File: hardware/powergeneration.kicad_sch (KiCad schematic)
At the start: 36 parts, among them U11 TPS55340PWPR, U5 AOZ1284PI, U6 TL431BIDBZR

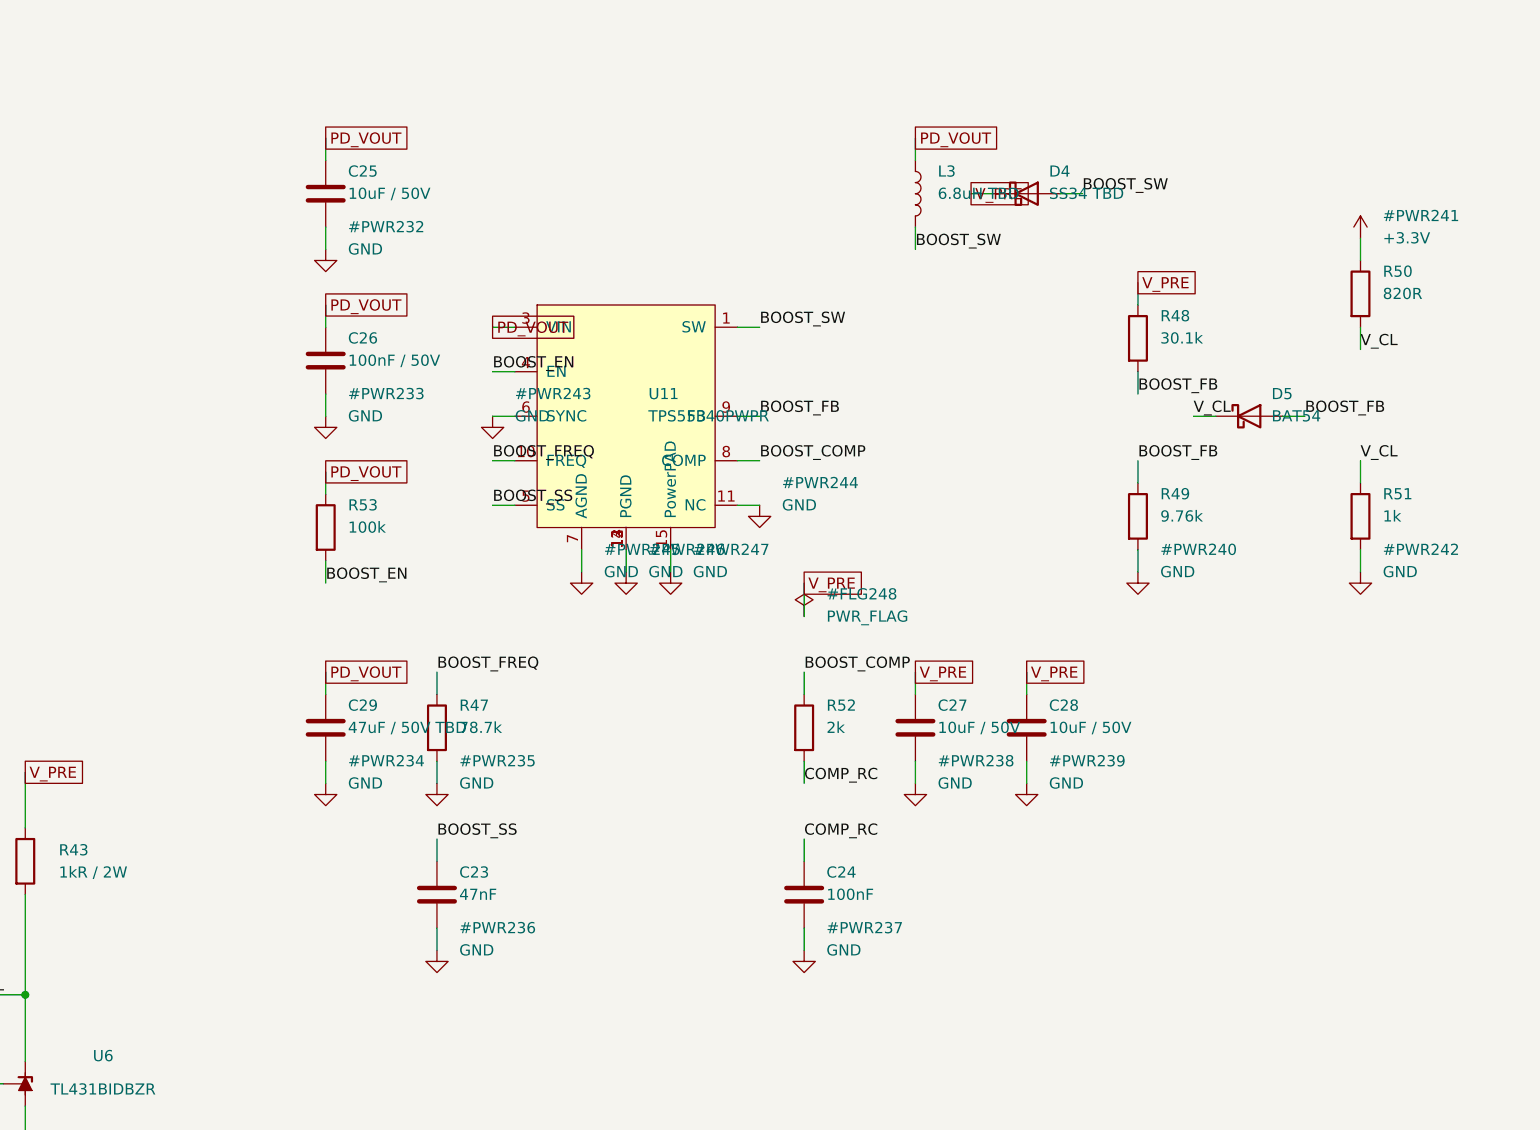
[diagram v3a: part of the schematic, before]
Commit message: powergeneration: Blok A'yı kistack/schematic skill kurallarına göre yeniden çiz
Izgara + etiket dizilimi yerine gerçek şema yerleşimi. Netlist değişmedi,
ERC 4'te sabit (hepsi REV_C öncesinden).

Yerleşim
- Soldan sağa sinyal akışı: PD_VOUT rayı -> L3 -> BOOST_SW -> D4 -> V_PRE
- Pasifler IC pinlerine gerçek tellerle bağlandı (dekuplaj, SS, FREQ,
  kompanzasyon, EN pull-up). Etiket yalnızca sayfa/blok arası ve okunabilirlik
  düğümlerinde (BOOST_SW, BOOST_FB, V_CL).
- Güç sembolleri: GND aşağı, +3.3V yukarı bakıyor. Referansları (#PWR###)
  gizlendi, değerleri görünür.
- PWR_FLAG kaynağın yanına, D4 çıkışına kondu.
- U11'in AGND/PGND/PowerPAD pinleri tek GND sembolünde köprülendi.
- Renk kodu: PD_VOUT turuncu, BOOST_SW mor, V_PRE kırmızı.
- Blok kesikli dikdörtgen içine alınıp başlıklandırıldı.

Semboller
- Dirençler Device:R_Small_US
- Değerlerde birim: 100kR, 78.7kR, 47nF, 10uF 50V, 6.8uH
- TPS55340PWPR sembolünün kutusu genişletildi (alt pin adları yan pin
  adlarına giriyordu). 15 pinin numara->ad eşlemesi datasheet ile birebir
  doğrulandı, değişmedi.

Yöntem
kicad-cli ile PDF -> pdftoppm ile PNG -> görüntüyü inceleyip düzeltme
döngüsü, 6 tur. Her turda ERC + netlist ile deterministik doğrulama.

Co-Authored-By: Claude Opus 5 <noreply@anthropic.com>
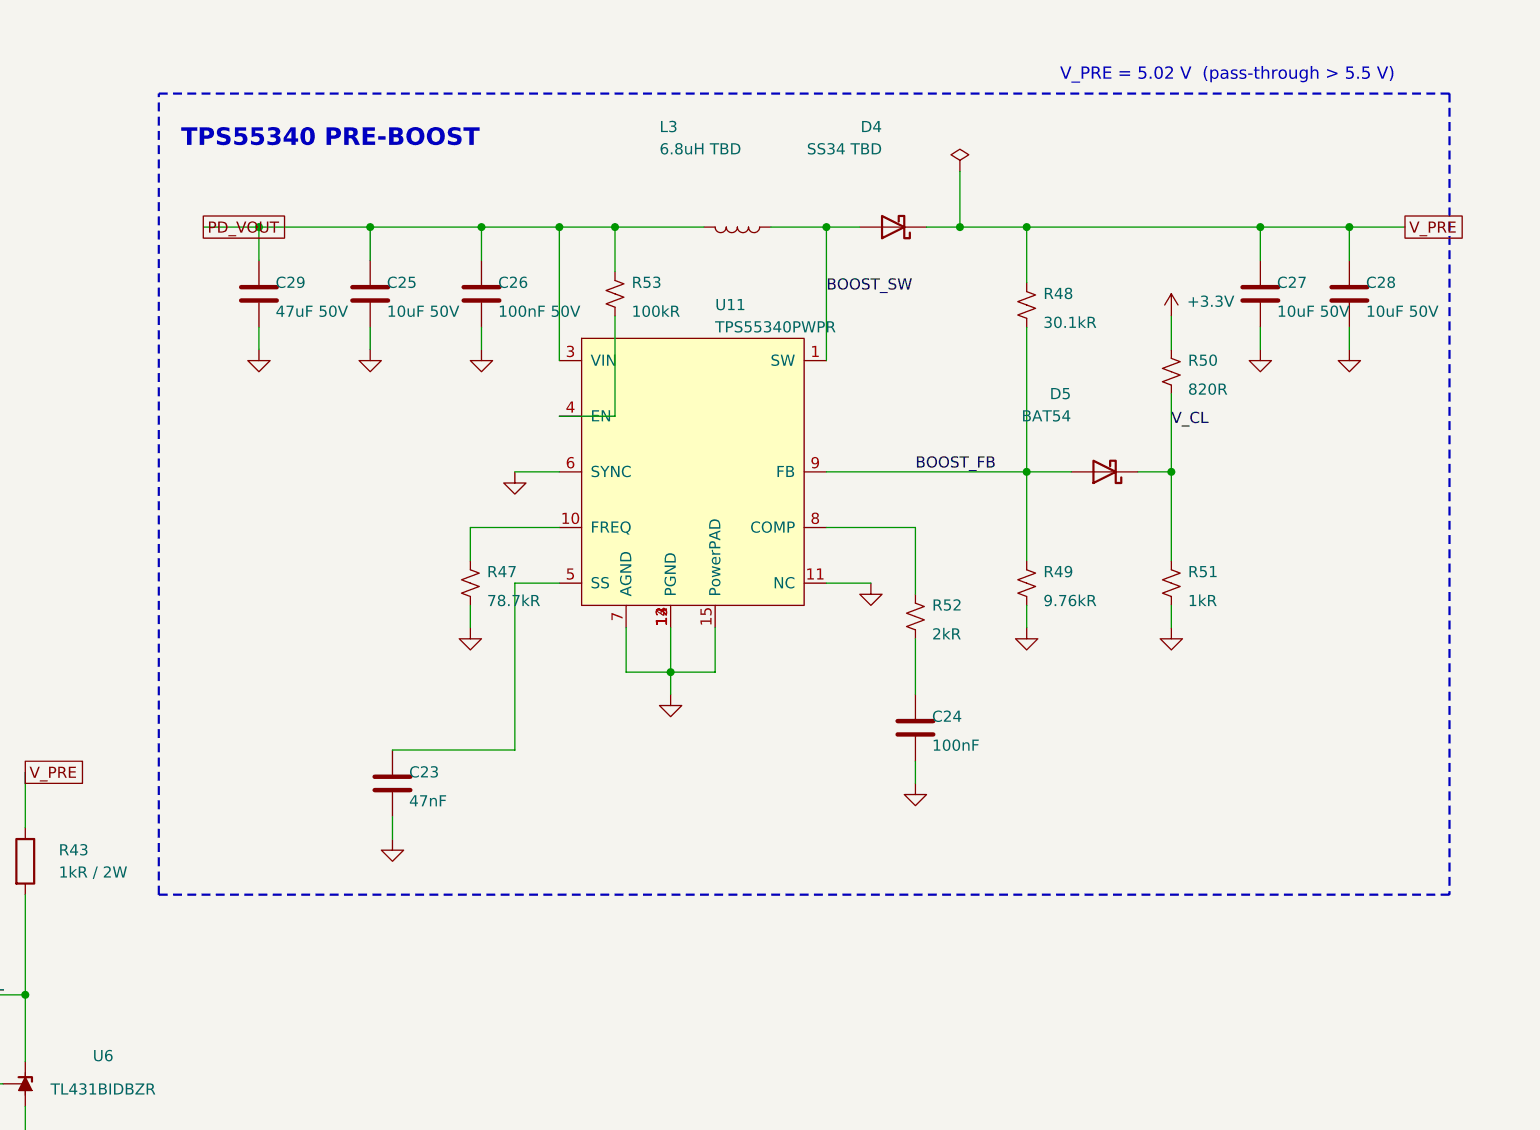
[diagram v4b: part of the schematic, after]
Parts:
- removed R47: 78.7k, Resistor_SMD:R_0402_1005Metric, symbol Device:R
- removed R48: 30.1k, Resistor_SMD:R_0402_1005Metric, symbol Device:R
- removed R49: 9.76k, Resistor_SMD:R_0402_1005Metric, symbol Device:R
- removed R50: 820R, Resistor_SMD:R_0402_1005Metric, symbol Device:R
- removed R51: 1k, Resistor_SMD:R_0402_1005Metric, symbol Device:R
- removed R52: 2k, Resistor_SMD:R_0402_1005Metric, symbol Device:R
- removed R53: 100k, Resistor_SMD:R_0402_1005Metric, symbol Device:R
- added R47: 78.7kR, Resistor_SMD:R_0402_1005Metric, symbol Device:R_Small_US
- added R48: 30.1kR, Resistor_SMD:R_0402_1005Metric, symbol Device:R_Small_US
- added R49: 9.76kR, Resistor_SMD:R_0402_1005Metric, symbol Device:R_Small_US
- added R50: 820R, Resistor_SMD:R_0402_1005Metric, symbol Device:R_Small_US
- added R51: 1kR, Resistor_SMD:R_0402_1005Metric, symbol Device:R_Small_US
- added R52: 2kR, Resistor_SMD:R_0402_1005Metric, symbol Device:R_Small_US
- added R53: 100kR, Resistor_SMD:R_0402_1005Metric, symbol Device:R_Small_US
- C25, C27, C28: value 10uF / 50V -> 10uF 50V
- C26: value 100nF / 50V -> 100nF 50V
- C29: value 47uF / 50V TBD -> 47uF 50V
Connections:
- net +3.3V: now also R50.1
- net BOOST_FB: now also R48.2, R49.1
- net BOOST_SW: now also L3.1; no longer L3.2
- net GND: now also R47.2, R49.2, R51.2
- net PD_VOUT: now also L3.2, R53.1; no longer L3.1
- net V_CL: now also R50.2, R51.1
- net V_PRE: now also R48.1
- net BOOST_COMP: no longer names the net of U11.8 (COMP)
- net BOOST_COMP: now also R52.1
- net BOOST_EN: no longer names the net of U11.4 (EN)
- net BOOST_EN: now also R53.2
- net BOOST_FREQ: no longer names the net of U11.10 (FREQ)
- net BOOST_FREQ: now also R47.1
- net BOOST_SS: no longer names the net of C23.1, U11.5 (SS)
- net COMP_RC: no longer names the net of C24.1
- net COMP_RC: now also R52.2
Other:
- note added: "TPS55340 PRE-BOOST"
- note added: "V_PRE = 5.02 V (pass-through > 5.5 V)"
